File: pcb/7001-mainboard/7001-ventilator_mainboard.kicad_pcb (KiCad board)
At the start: 2 copper layers, 65 x 56.5 mm, 142 parts, among them J1 USB_B_Micro, J10 6-pin header, J11 4-pin screw terminal, J12 3-pin screw terminal, J13 2-pin screw terminal, J14 2-pin screw terminal, J15 6-pin header, J2 4-pin header, J3 2-pin screw terminal, J4 DNI, J5 2-pin screw terminal, J6 5V out, J7 2-pin screw terminal, J8 3-pin screw terminal, J9 Raspberry_Pi_2_3, U1 MPRLS0001PG0000SA, U10 ABPMAND001PG2A3, U11 MPVZ5010GW6U, U12 MPVZ5010GW6U, U13 ITS4142NHUMA1, U14 ITS4142NHUMA1, U2 TPD2E2U06, U3 LPC11U37FBD48-401_, U4 MCP1825S-3302E, U5 S24SE05004PDFA_DC-DC, U6 LM2937IMP-12/NOPB, U7 AD5410AREZ, U8 MPRLS0001PG0000SA, U9 ABPMAND001PG2A3, Y1 12MHz

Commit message: Finalize BOM, add all footprints
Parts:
- added D11: D_TVS, Jitter_Footprints:WE-TVSP_TVS_DIODE, F.Cu at (124.2, 17.9)
- added D3: S5MB R5G 100V, Diode_SMD:D_SMB, F.Cu at (114.8, 27.3)
- added D4: D_TVS, Jitter_Footprints:WE-TVSP_TVS_DIODE, F.Cu at (115.1, 17.9)
- added D5: D_TVS, Jitter_Footprints:WE-TVSP_TVS_DIODE, F.Cu at (115.1, 22.3)
- added FL1: 744282010, Jitter_Footprints:L_CommonMode_Wuerth_WE-SCC, F.Cu at (111.5, 5.00)
- added J16: 10-pin SWD header, Jitter_Footprints:connector_jtag_10pin_shrouded, F.Cu at (106.4, 23.1)
- added RV1: Varistor, Jitter_Footprints:WE_VS_Varistor, F.Cu at (122.4, 21.7)
- J15: value 6-pin header -> 2x10-pin header
- J9: footprint Connector_PinSocket_2.54mm:PinSocket_2x20_P2.54mm_Vertical -> Jitter_Footprints:PinSocket_2x20_P2.54mm_Vertical_holes_SMD; moved to F.Cu
- moved J9 0.07 mm to (108.3, 105.2), turned to 90 degrees
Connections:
- net /pressure_sensor/PSENSE_RESET renamed /PSENSE_RESET
- C47 pad 1: (no net) -> Net-(C47-Pad1)
- J2 pad 4: (no net) -> +3V3

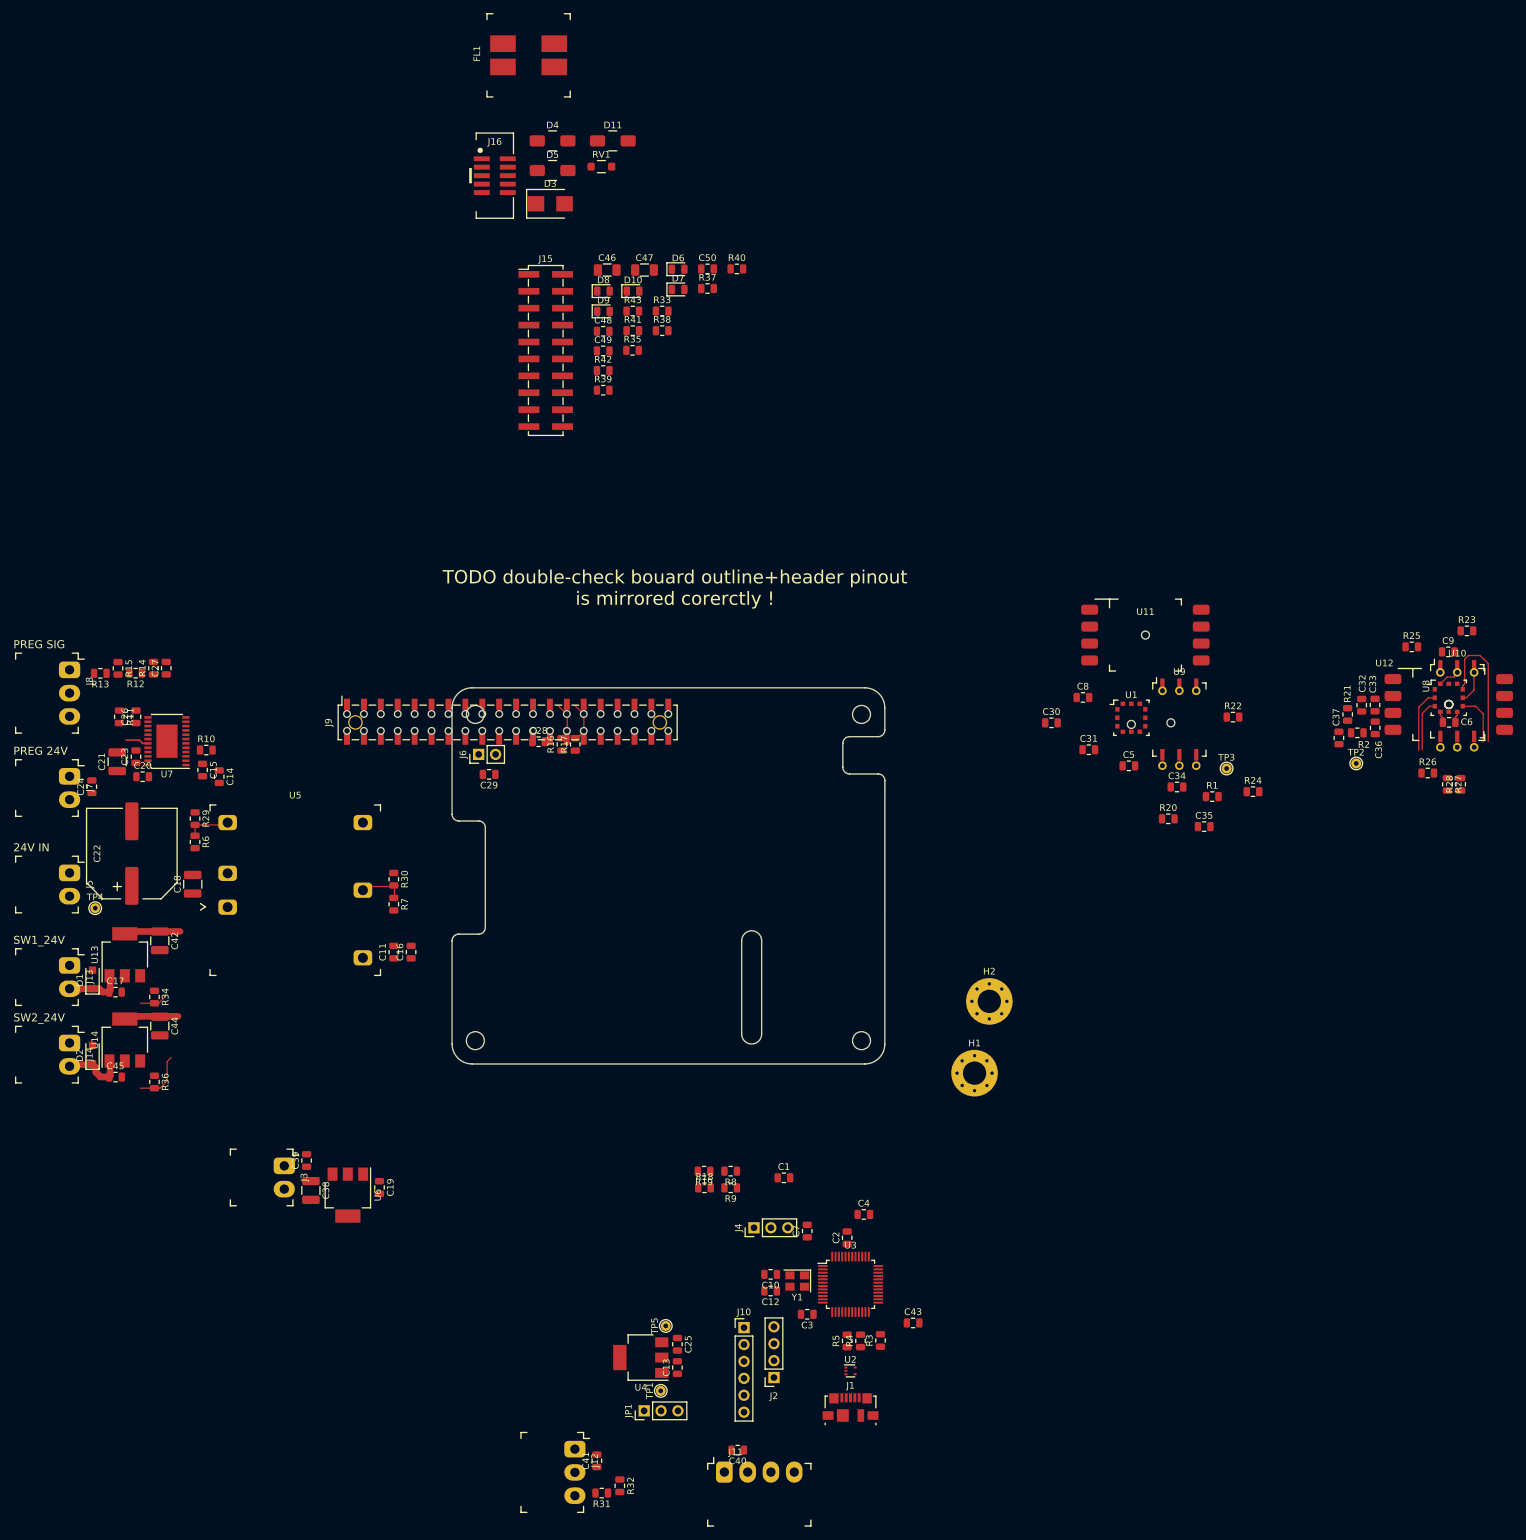
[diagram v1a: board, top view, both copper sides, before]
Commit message: PCB: Halfway layouting
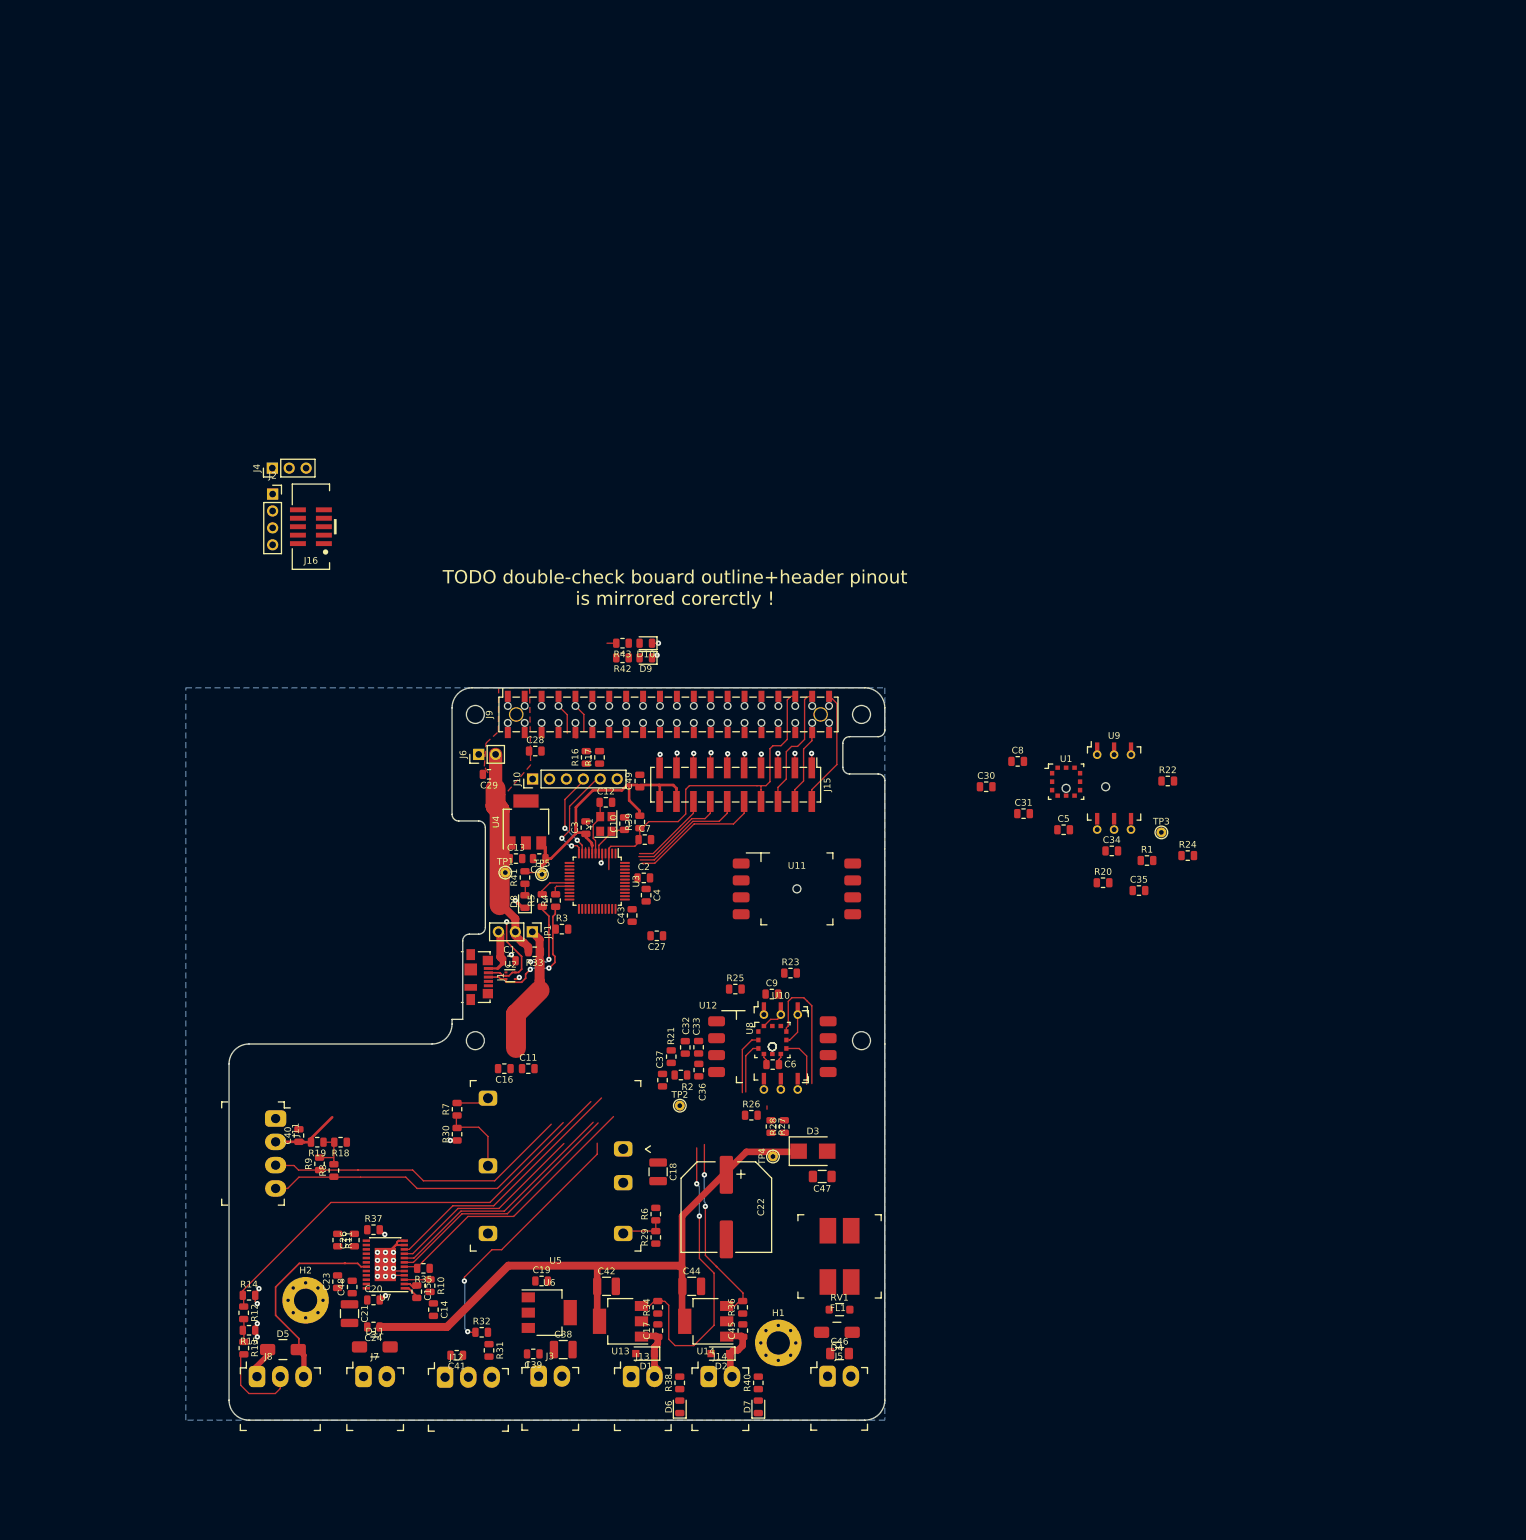
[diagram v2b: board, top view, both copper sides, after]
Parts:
- removed C50: 100nF, Capacitor_SMD:C_0805_2012Metric
- moved FL1 186.3 mm to (158.2, 185.4), turned to 180 degrees
- moved D11 184.6 mm to (88.4, 199.0)
- moved D4 184.0 mm to (157.8, 196.8), turned to 180 degrees
- moved D5 181.7 mm to (74.6, 199.4)
- moved RV1 175.4 mm to (158.2, 193.4)
- moved D6 170.9 mm to (134.2, 208.0), turned to 90 degrees
- moved D7 168.3 mm to (146.0, 208.0), turned to 90 degrees
- moved R40 167.4 mm to (146.0, 204.4), turned to 90 degrees
- moved C46 166.4 mm to (158.2, 200.0)
- moved R38 158.1 mm to (134.2, 204.4), turned to 90 degrees
- moved J2 152.6 mm to (73.0, 70.9), turned to 0 degrees
- moved R37 150.0 mm to (88.2, 181.4)
- moved C48 148.4 mm to (85.0, 190.0), turned to 90 degrees
- moved D3 147.7 mm to (154.2, 169.6)
- moved R35 141.4 mm to (95.7, 187.2), turned to 180 degrees
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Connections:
- C37 pad 1: /A_PRESSURE_1 -> /A_PRESSURE_2
- J10 pad 4: (no net) -> /UART_RX
- J10 pad 5: (no net) -> /UART_TX
- J15 pad 10: (no net) -> /MCU_IO_4
- J15 pad 12: (no net) -> /MCU_IO_3
- J15 pad 14: (no net) -> /MCU_IO_2
- J15 pad 16: (no net) -> /MCU_IO_1
- J15 pad 18: (no net) -> +3V3
- J15 pad 2: +3V3 -> /RPI_IO_3
- J15 pad 4: (no net) -> /RPI_IO_2
- J15 pad 6: (no net) -> /RPI_IO_1
- J15 pad 8: (no net) -> /~RESET~
- J5 pad 1: Net-(C46-Pad2) -> Net-(C46-Pad1)
- J5 pad 2: Net-(C46-Pad1) -> Net-(C46-Pad2)
- J9 pad 36: (no net) -> /~RESET~
- J9 pad 37: (no net) -> /RPI_IO_2
- J9 pad 38: (no net) -> /RPI_IO_1
- J9 pad 40: (no net) -> /RPI_IO_3
- R2 pad 1: /A_PRESSURE_1 -> /A_PRESSURE_2
- R21 pad 2: /A_PRESSURE_1 -> /A_PRESSURE_2
- R42 pad 2: (no net) -> /LED_STATUS
- R43 pad 2: (no net) -> /LED_ERROR
- TP3 pad 1: /A_PRESSURE_1 -> /A_PRESSURE_2
- U1 pad 1: (no net) -> /PSENSE_1_SPI_~CS~
- U3 pad 1: (no net) -> /MCU_IO_1
- U3 pad 10: (no net) -> /LED_ERROR
- U3 pad 13: (no net) -> /PSENSE_RESET
- U3 pad 18: (no net) -> /PSENSE_2_DATA_READY
- U3 pad 21: (no net) -> /PSENSE_2_SPI_~CS~
- U3 pad 22: (no net) -> /PSENSE_1_SPI_~CS~
- U3 pad 23: (no net) -> /PSENSE_1_DATA_READY
- U3 pad 24: (no net) -> /PREG_OK
- U3 pad 25: (no net) -> /PREG_SPI_~CS~
- U3 pad 26: (no net) -> /PREG_SPI_MISO
- U3 pad 27: (no net) -> /PSENSE_SPI_MISO
- U3 pad 28: (no net) -> /PSENSE_SPI_MOSI
- U3 pad 31: (no net) -> /PSENSE_SPI_CLK
- U3 pad 32: (no net) -> /A_PREG_PRESSURE
- U3 pad 33: (no net) -> /A_FLOW
- U3 pad 34: (no net) -> /A_PRESSURE_1
- U3 pad 35: (no net) -> /A_PRESSURE_2
- U3 pad 36: (no net) -> /MCU_IO_1
- U3 pad 38: (no net) -> /PREG_SPI_MOSI
- U3 pad 42: (no net) -> /PREG_CLEAR
- U3 pad 43: (no net) -> /PREG_SPI_CLK
- U3 pad 45: (no net) -> /MCU_IO_4
- U3 pad 46: (no net) -> /MCU_IO_3
- U3 pad 47: (no net) -> /MCU_IO_2
- U3 pad 9: (no net) -> /LED_STATUS
- U7 pad 10: (no net) -> /PREG_SPI_MISO
- U7 pad 7: (no net) -> /PREG_SPI_~CS~
- U7 pad 8: (no net) -> /PREG_SPI_CLK
- U7 pad 9: (no net) -> /PREG_SPI_MOSI
- U8 pad 1: (no net) -> /PSENSE_2_SPI_~CS~
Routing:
- net +24V: track 17.1 -> 95.9 mm
- net /A_PREG_PRESSURE: track 0.00 -> 66.4 mm
- net GND: track 0.00 -> 53.0 mm, vias 0 -> 35
- net +3V3: track 0.00 -> 52.8 mm
- net /~RESET~: track 0.00 -> 52.5 mm
- net /I2C_SCL: track 0.00 -> 48.7 mm
- net /I2C_SDA: track 0.00 -> 46.2 mm
- net +5V: track 0.00 -> 43.3 mm
- net /switch_1_out: track 4.45 -> 45.5 mm, vias 0 -> 2
- net /PREG_CLEAR: track 0.00 -> 40.8 mm
- net /PREG_SPI_MISO: track 0.00 -> 39.0 mm
- net /A_FLOW: track 0.00 -> 38.8 mm, vias 0 -> 2
- net /PREG_SPI_~CS~: track 0.00 -> 37.8 mm
- net /PREG_SPI_CLK: track 0.00 -> 36.8 mm
- net /PREG_SPI_MOSI: track 0.00 -> 30.8 mm
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- added copper zone on F.Cu, net +5V
- added copper zone on B.Cu, net GND
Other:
- board size 65 x 56.5 mm -> 98.5 x 110 mm
- board text removed: "24V IN"
- board text removed: "PREG 24V"
- board text removed: "PREG SIG"
- board text removed: "SW1_24V"
- board text removed: "SW2_24V"

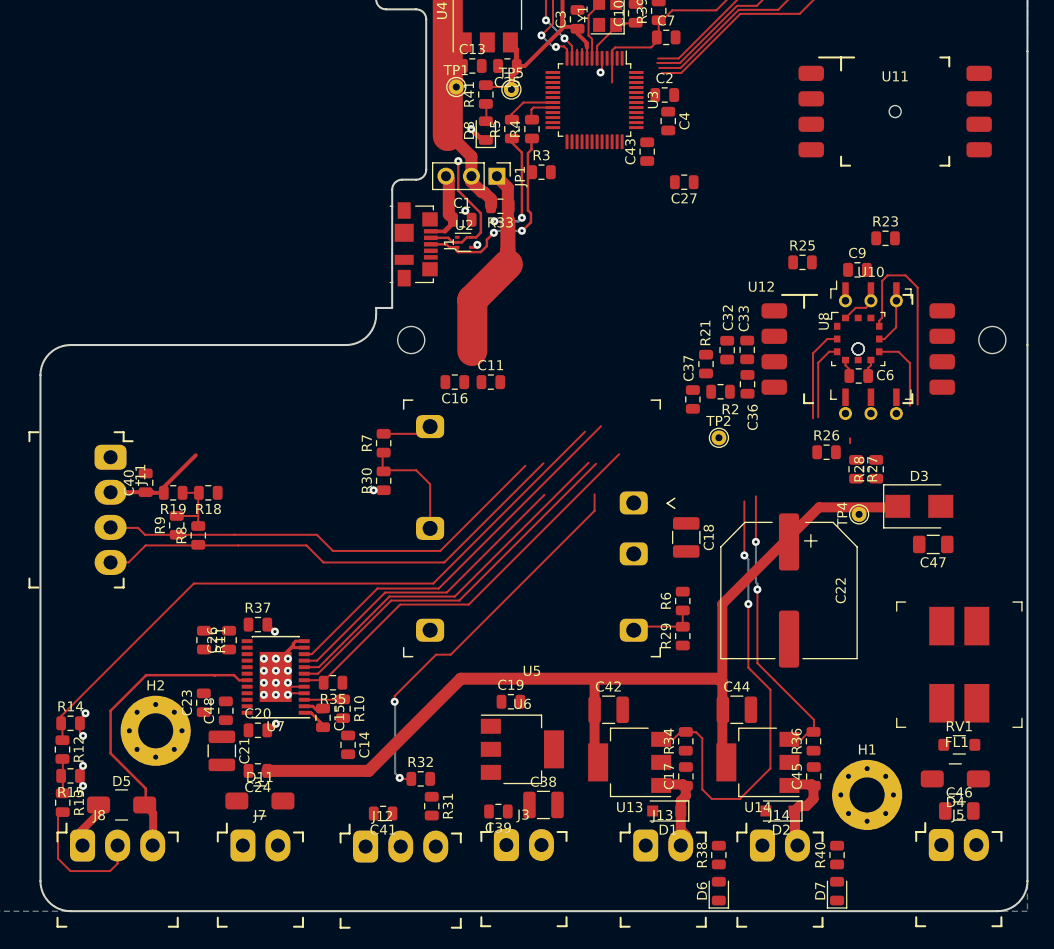
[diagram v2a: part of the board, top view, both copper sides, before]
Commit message: PCB: route bottom half
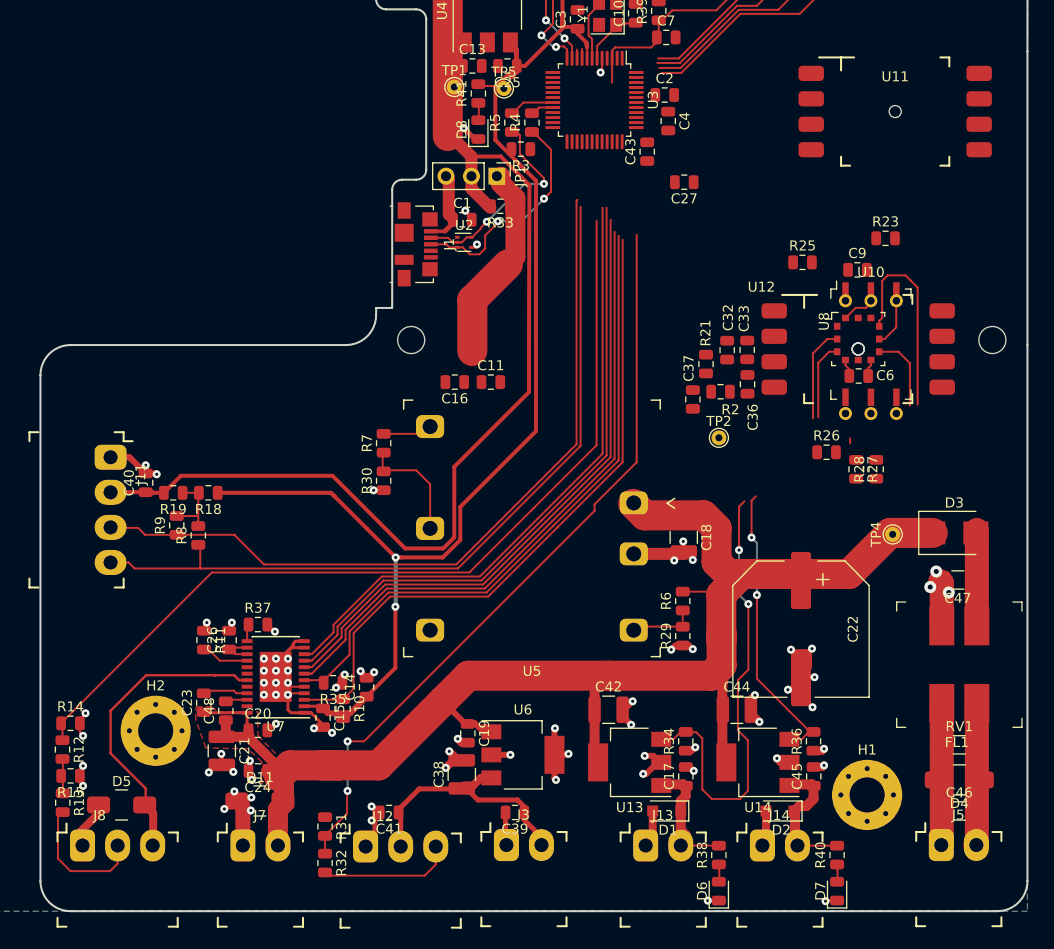
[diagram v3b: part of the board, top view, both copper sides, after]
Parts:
- moved R32 12.7 mm to (94.9, 205.2), turned to 270 degrees
- moved R31 10.8 mm to (94.9, 201.6)
- moved C38 8.70 mm to (108.5, 196.3), turned to 90 degrees
- moved C14 6.04 mm to (99.0, 187.7), turned to 90 degrees
- moved C19 5.33 mm to (109.2, 192.2), turned to 270 degrees
- moved D3 4.39 mm to (157.7, 172.2)
- moved C47 4.31 mm to (158.1, 176.9)
- moved C22 4.03 mm to (142.4, 181.8)
- moved TP4 3.90 mm to (151.6, 172.4)
- moved R3 3.08 mm to (114.5, 133.9), turned to 180 degrees
- moved C39 1.65 mm to (113.8, 200.2)
- moved D8 0.76 mm to (110.2, 132.0)
- moved R41 0.76 mm to (110.2, 128.4)
- moved TP5 0.76 mm to (112.8, 127.9)
- moved R4 0.65 mm to (115.5, 131.3)
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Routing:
- net GND: track 53.0 -> 165.2 mm, vias 35 -> 89
- net +3V3: track 52.8 -> 154.1 mm, vias 0 -> 2
- net +24V: track 95.9 -> 174.1 mm
- net +5V: track 43.3 -> 117.0 mm
- net /PREG_OK: track 3.88 -> 67.0 mm
- net /A_FLOW: track 38.8 -> 75.6 mm
- net /PREG_SPI_MOSI: track 30.8 -> 63.9 mm
- net /I2C_SDA: track 46.2 -> 77.8 mm
- net /I2C_SCL: track 48.7 -> 78.2 mm
- net /PREG_SPI_CLK: track 36.8 -> 63.5 mm
- net /PREG_SPI_~CS~: track 37.8 -> 63.1 mm
- net +12V: track 0.00 -> 24.2 mm
- net /PREG_SPI_MISO: track 39.0 -> 63.1 mm
- net /PREG_CLEAR: track 40.8 -> 64.2 mm
- net /A_PREG_PRESSURE: track 66.4 -> 89.0 mm
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- added copper zone on F.Cu, net +24V

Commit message: update layout
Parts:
- moved J4 106.2 mm to (133.8, 154.1), turned to 270 degrees
- moved J2 99.9 mm to (133.8, 150.2), turned to 180 degrees
- moved J16 85.2 mm to (128.1, 145.3), turned to 0 degrees
- moved C27 54.0 mm to (95.0, 177.8), turned to 270 degrees
- moved R43 39.8 mm to (130.6, 132.8), turned to 90 degrees
- moved D10 39.5 mm to (133.3, 132.6)
- moved D9 34.1 mm to (135.2, 129.1), turned to 0 degrees
- moved R42 32.7 mm to (134.2, 127.0)
- moved C37 22.9 mm to (147.4, 142.3), turned to 0 degrees
- moved R23 22.5 mm to (163.4, 161.5), turned to 270 degrees
- moved R21 21.5 mm to (150.9, 143.6), turned to 180 degrees
- moved TP2 20.1 mm to (143.5, 144.9), turned to 270 degrees
- moved C43 20.1 mm to (123.5, 154.0), turned to 0 degrees
- moved C32 19.1 mm to (152.3, 145.7), turned to 180 degrees
- moved R2 19.0 mm to (148.1, 145.1), turned to 270 degrees
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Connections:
- J4 pad 2: /~ISP~ -> /~RESET~
- J4 pad 3: /~RESET~ -> /~ISP~
- U3 pad 1: /MCU_IO_1 -> /PSENSE_2_SPI_~CS~
- U3 pad 10: /LED_ERROR -> (no net)
- U3 pad 2: (no net) -> /PSENSE_1_SPI_~CS~
- U3 pad 21: /PSENSE_2_SPI_~CS~ -> (no net)
- U3 pad 22: /PSENSE_1_SPI_~CS~ -> (no net)
- U3 pad 23: /PSENSE_1_DATA_READY -> /PREG_CLEAR
- U3 pad 40: (no net) -> /PSENSE_1_DATA_READY
- U3 pad 42: /PREG_CLEAR -> /LED_ERROR
- U3 pad 45: /MCU_IO_4 -> /LED_STATUS
- U3 pad 46: /MCU_IO_3 -> /MCU_IO_4
- U3 pad 47: /MCU_IO_2 -> /MCU_IO_3
- U3 pad 48: (no net) -> /MCU_IO_2
- U3 pad 9: /LED_STATUS -> (no net)
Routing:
- net GND: track 165.2 -> 226.8 mm, vias 89 -> 132
- net +3V3: track 154.1 -> 204.5 mm, vias 2 -> 6
- net /switch_1_out: track 45.0 -> 93.3 mm, vias 2 -> 4
- net /switch_2_out: track 28.6 -> 73.4 mm
- net /~RESET~: track 52.5 -> 86.3 mm, vias 0 -> 2
- net /~ISP~: track 0.00 -> 33.6 mm, vias 0 -> 2
- net /PSENSE_2_DATA_READY: track 5.89 -> 34.8 mm, vias 0 -> 2
- net /PSENSE_RESET: track 20.6 -> 49.4 mm, vias 0 -> 2
- net /SWCLK: track 0.00 -> 23.8 mm, vias 0 -> 2
- net /I2C_SCL: track 78.2 -> 100.5 mm, vias 0 -> 4
- net /PSENSE_SPI_MISO: track 7.77 -> 29.9 mm, vias 0 -> 2
- net /I2C_SDA: track 77.8 -> 99.4 mm, vias 0 -> 2
- net /SWDIO: track 0.00 -> 20.9 mm, vias 0 -> 2
- net /PSENSE_SPI_CLK: track 7.79 -> 27.2 mm, vias 0 -> 2
- net /PREG_SPI_CLK: track 63.5 -> 82.5 mm, vias 0 -> 2
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- added copper zone on F.Cu, net GND
